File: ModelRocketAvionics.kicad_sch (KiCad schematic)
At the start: 68 parts, among them P1 USB_C_Plug, Q2 AO3400A, Q3 AO3400A, SW2 SW_SPDT, U1 ICM-42605, U2 W25Q16JVSS, U3 BMP280, U5 STM32F411, U6 L86-M33, U7 915MHz, U9 AP7361C-33E, X1 Shenzhen SCTF Elec SX2B12.000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

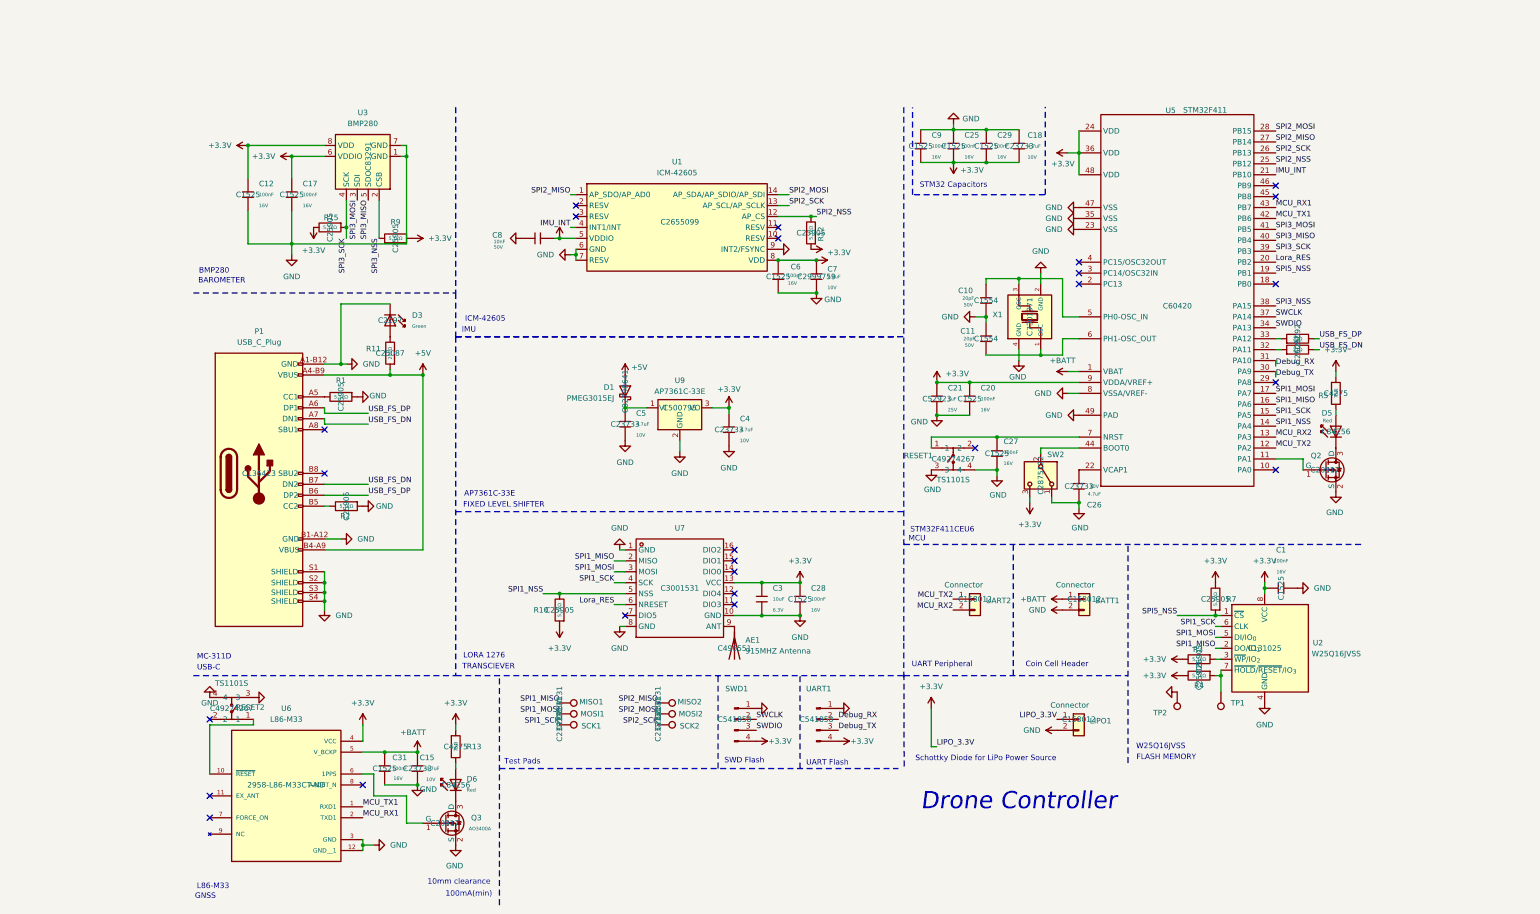
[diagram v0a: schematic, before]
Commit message: Basic layout and routing, modified schematic, and directory
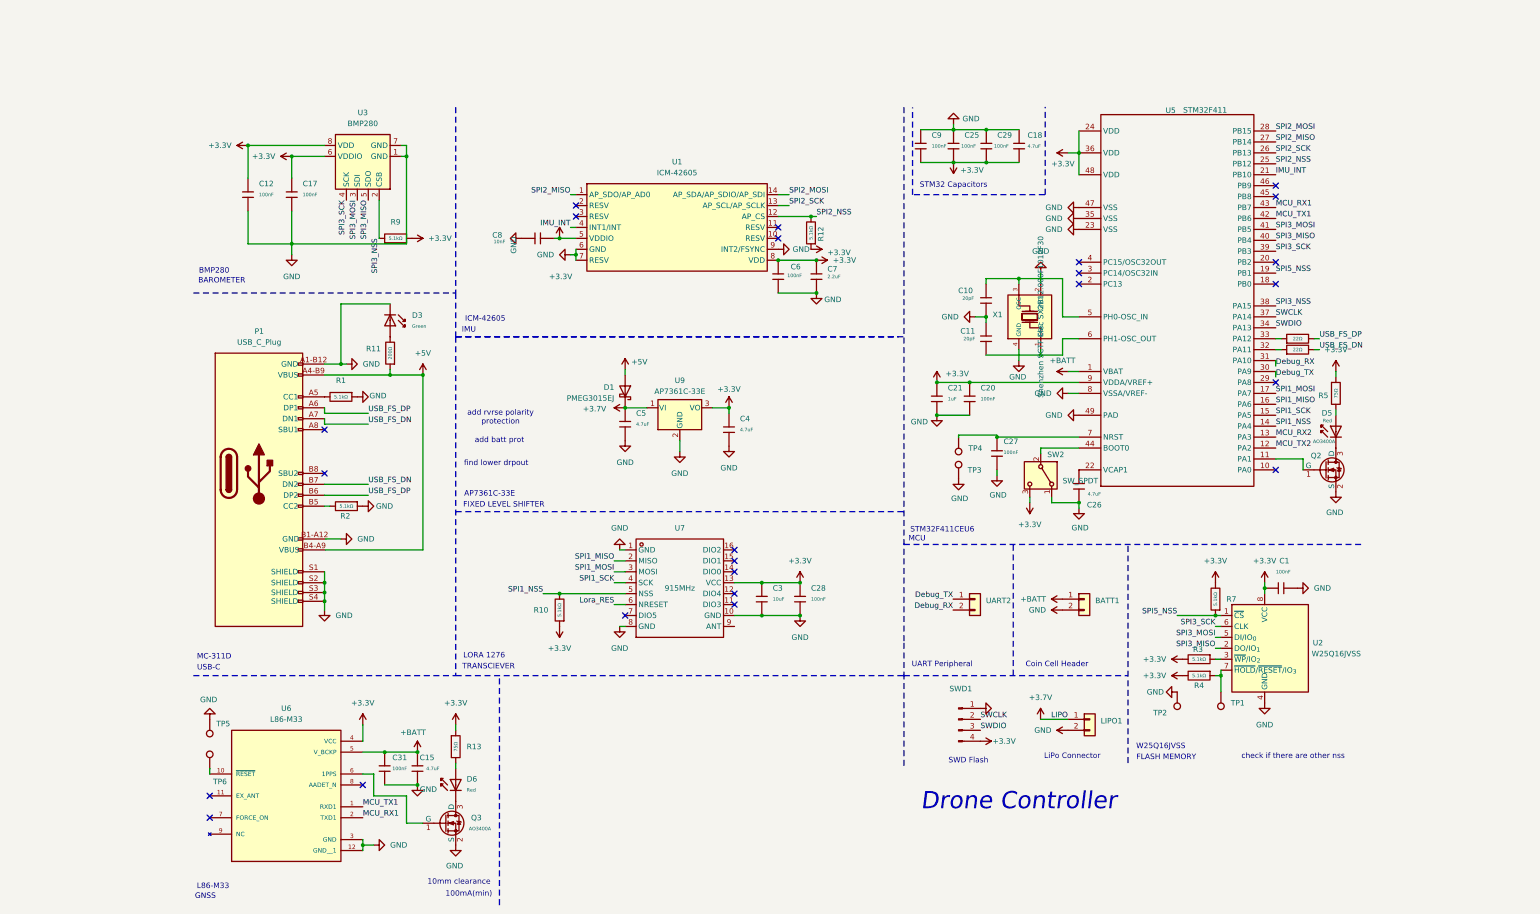
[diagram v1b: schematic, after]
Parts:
- removed AE1: 915MHZ Antenna, Connector_Coaxial:SMA_BAT_Wireless_BWSMA-KWE-Z001, symbol Device:Antenna
- removed MISO1, MISO2, MOSI1, MOSI2, SCK1, SCK2: TestPoint, TestPoint:TestPoint_Keystone_5019_Miniature, symbol Connector:TestPoint
- removed R15: 5.1kΩ, PCM_JLCPCB:R_0402, symbol PCM_JLCPCB-Resistors:0402,5.1kΩ
- removed RESET1, RESET2: TS1101S, easyeda2kicad:SW-SMD_4P-L4.5-W4.5-P3.15-LS7.5-TL, symbol easyeda2kicad:TS1101S-4.5X4.5X5.5FSS
- removed UART1: Conn_01x04_Pin, Connector_PinHeader_2.00mm:PinHeader_1x04_P2.00mm_Vertical, symbol Connector:Conn_01x04_Pin
- added TP3, TP4, TP5, TP6: TestPoint, symbol Connector:TestPoint
- P1: footprint USB-C:USB-C -> Connector_USB:USB_C_Receptacle_GCT_USB4105-xx-A_16P_TopMnt_Horizontal
- R1, R10, R11, R12, R14, R2, R3, R4, R6, R7, R9: footprint PCM_JLCPCB:R_0402 -> Resistor_SMD:R_0402_1005Metric
- R13, R5: footprint PCM_JLCPCB:R_0603 -> Resistor_SMD:R_0603_1608Metric
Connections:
- net +3.3V: no longer LIPO1.1 (Pin_1)
- net Debug_RX: now also UART2.2 (Pin_2)
- net Debug_TX: now also UART2.1 (Pin_1)
- net GND: now also TP3.1, TP5.1
- net Lora_RES: no longer U5.20 (PB2)
- net MCU_RX2: no longer UART2.2 (Pin_2)
- net MCU_TX2: no longer UART2.1 (Pin_1)
- net SPI1_MISO: no longer U2.2 (DO/IO_{1})
- net SPI1_MOSI: no longer U2.5 (DI/IO_{0})
- net SPI1_SCK: no longer U2.6 (CLK)
- net SPI3_MISO: now also U2.2 (DO/IO_{1})
- net SPI3_MOSI: now also U2.5 (DI/IO_{0})
- net SPI3_SCK: now also U2.6 (CLK)
- net at C27.1, U5.7 (NRST): now also TP4.1
- net +3.7V: now reaches C5.1, D1.1 (K), U9.1 (VI)
- net +3.7V: now also LIPO1.1 (Pin_1)
- net at U6.10 (~{RESET}): now also TP6.1
- no-connect marks 25 -> 24
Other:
- note added: "LiPo Connector"
- note added: "add batt prot"
- note added: "add rvrse polarity protection"
- note added: "check if there are other nss"
- note added: "find lower drpout"
- note removed: "Schottky Diode for LiPo Power Source"
- note removed: "Test Pads"
- note removed: "UART Flash"
- moved on the sheet: LIPO1, SWD1

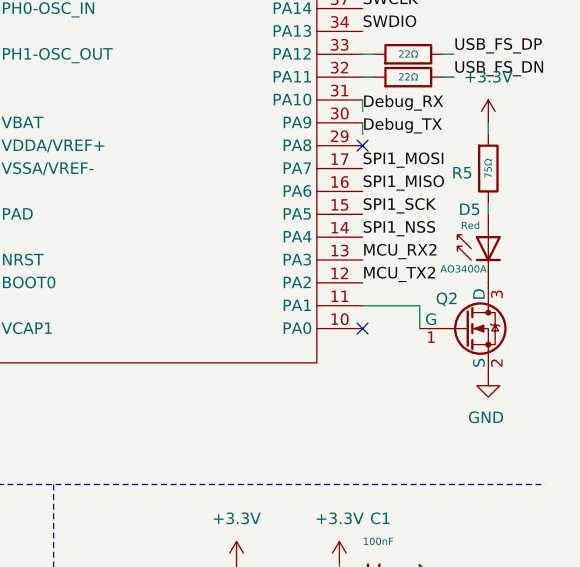
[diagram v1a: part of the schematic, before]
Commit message: Added more room for antenna pin on LoRa
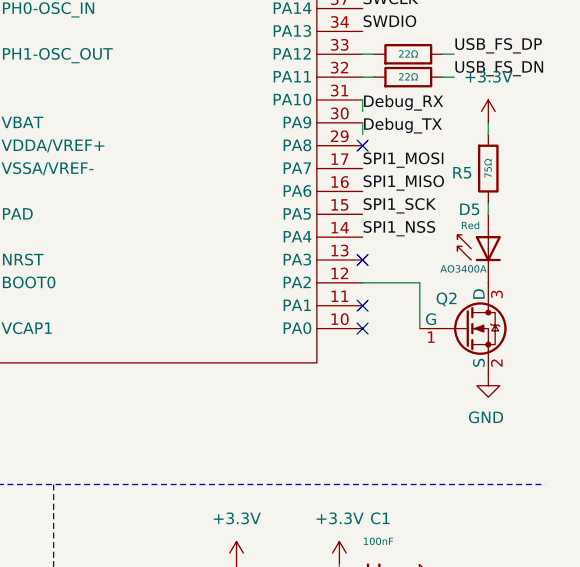
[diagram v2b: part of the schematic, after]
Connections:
- net at U5.11 (PA1): no longer Q2.1 (G)
- net MCU_RX2: no longer names the net of U5.13 (PA3)
- net MCU_TX2: no longer names the net of U5.12 (PA2)
- net MCU_TX2: now also Q2.1 (G)
- no-connect marks 24 -> 26
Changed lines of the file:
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@@
+	)
+	(no_connect
+		(at 264.1968 94.4382)
 	)
 	(no_connect
@@
 	)
 	(no_connect
+		(at 264.1968 89.3582)
+	)
+	(no_connect
 		(at 148.59 43.18)
 	)
@@
 	(wire
 		(pts
-			(xy 264.1968 94.4382) (xy 270.5468 94.4382)
-		)
-		(stroke
-			(width 0)
-			(type default)
-		)
-	)
-	(wire
-		(pts
 			(xy 111.76 115.57) (xy 113.03 115.57)
 		)
@@
 	(wire
 		(pts
-			(xy 270.5468 96.9782) (xy 270.5468 94.4382)
-		)
-		(stroke
-			(width 0)
-			(type default)
-		)
-	)
-	(wire
-		(pts
 			(xy 185.4568 84.2782) (xy 193.0768 84.2782)
 		)
@@
 		)
 	)
+	(wire
+		(pts
+			(xy 270.5468 91.8982) (xy 270.5468 96.9782)
+		)
+		(stroke
+			(width 0)
+			(type default)
+		)
+	)
 	(polyline
 		(pts
@@
 		(pts
 			(xy 204.5068 52.5282) (xy 214.6668 52.5282)
+		)
+		(stroke
+			(width 0)
+			(type default)
+		)
+	)
+	(wire
+		(pts
+			(xy 270.5468 91.8982) (xy 264.1968 91.8982)
 		)
 		(stroke
@@
 		)
 	)
-	(label "MCU_RX2"
-		(at 264.1968 89.3582 0)
-		(effects
-			(font
-				(size 1.27 1.27)
-			)
-			(justify left bottom)
-		)
-	)
 	(label "SPI1_SCK"
 		(at 110.49 123.19 180)
@@
 		(effects
 			(font
-				(size 1.27 1.27)
-			)
-			(justify left bottom)
-		)
-	)
-	(label "MCU_TX2"
-		(at 264.1968 91.8982 0)
-		(effects
-			(font

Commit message: Added RP2040 compatible branch, addded battery protection circuitry
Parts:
- removed C10, C11: 20pF, PCM_JLCPCB:C_0402, symbol PCM_JLCPCB-Capacitors:0402,20pF
- removed C18, C26: 4.7uF, PCM_JLCPCB:C_0402, symbol PCM_JLCPCB-Capacitors:0402,4.7uF
- removed C21: 1uF, PCM_JLCPCB:C_0402, symbol PCM_JLCPCB-Capacitors:0402,1uF
- removed C27: 100nF, PCM_JLCPCB:C_0402, symbol PCM_JLCPCB-Capacitors:0402,100nF
- removed D5: Red, PCM_JLCPCB:D_0805, symbol PCM_JLCPCB-Diodes:LED,0805,Red
- removed Q2: AO3400A, PCM_JLCPCB:Q_SOT-23, symbol PCM_JLCPCB-Transistors:NMOS,AO3400A
- removed R14, R6: 22Ω, Resistor_SMD:R_0402_1005Metric, symbol PCM_JLCPCB-Resistors:0402,22Ω
- removed R3, R4: 5.1kΩ, Resistor_SMD:R_0402_1005Metric, symbol PCM_JLCPCB-Resistors:0402,5.1kΩ
- removed R5: 75Ω, Resistor_SMD:R_0603_1608Metric, symbol PCM_JLCPCB-Resistors:0603,75Ω
- removed TP3, TP4: TestPoint, symbol Connector:TestPoint
- removed U5: STM32F411, Package_DFN_QFN:QFN-48-1EP_7x7mm_P0.5mm_EP5.6x5.6mm, symbol STM32:STM32F411CEU6
- removed X1: Shenzhen SCTF Elec SX2B12.000F1010F30, Crystal:Crystal_SMD_2520-4Pin_2.5x2.0mm, symbol PCM_JLCPCB-Crystals:Crystal, 12MHz, 20pF
- added C10, C11: 15pF, PCM_JLCPCB:C_0402, symbol PCM_JLCPCB-Capacitors:0402,15pF
- added C13, C14, C16, C18, C19, C2: 100nF, PCM_JLCPCB:C_0402, symbol PCM_JLCPCB-Capacitors:0402,100nF
- added C22, C23: 1uF, PCM_JLCPCB:C_0402, symbol PCM_JLCPCB-Capacitors:0402,1uF
- added D2: Red, PCM_JLCPCB:D_0805, symbol PCM_JLCPCB-Diodes:LED,0805,Red
- added JP1: Jumper_2_Open, symbol Jumper:Jumper_2_Open
- added Q1: AO3400A, PCM_JLCPCB:Q_SOT-23, symbol PCM_JLCPCB-Transistors:NMOS,AO3400A
- added Q2: NCE8205, easyeda2kicad:SOT-23-6_L2.9-W1.6-P0.95-LS2.8-BL, symbol easyeda2kicad:NCE8205
- added R16: 75Ω, Resistor_SMD:R_0603_1608Metric, symbol PCM_JLCPCB-Resistors:0603,75Ω
- added R17, R18: 27Ω, PCM_JLCPCB:R_0603, symbol PCM_JLCPCB-Resistors:0603,27Ω
- added R3: FM2113_C2832124, easyeda2kicad:SOT-23-6_L2.9-W1.6-P0.95-LS2.8-BR, symbol easyeda2kicad:FM2113_C2832124
- added R4: 2kΩ, PCM_JLCPCB:R_0402, symbol PCM_JLCPCB-Resistors:0402,2kΩ
- added U4: RP2040, Package_DFN_QFN:QFN-56-1EP_7x7mm_P0.4mm_EP3.2x3.2mm, symbol MCU_RaspberryPi:RP2040
- added X1: Crystal_GND24_Small, Crystal:Crystal_SMD_3225-4Pin_3.2x2.5mm, symbol Device:Crystal_GND24_Small
- C20: LCSC (none) -> C1525; LCSC Part Number C1525 -> (none); Manufacturer (none) -> Samsung Electro-Mechanics; Minimum Qty (none) -> 20; Stock 24076106 -> 20208285
- SWD1: footprint Connector_PinHeader_2.00mm:PinHeader_1x04_P2.00mm_Vertical -> Connector_PinHeader_2.00mm:PinHeader_2x02_P2.00mm_Vertical
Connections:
- net SPI2_SCK is gone; now on net SPI1_SCK: U1.13 (AP_SCL/AP_SCLK)
- net SPI3_NSS is gone; now on net SPI0_CSn: R9.1, U3.2 (CSB)
- net +3.3V: now also C25.1, C29.1, C9.1, C13.1, C14.1, C16.1, C2.1, C23.1, R16.1, U4.1 (IOVDD), U4.10 (IOVDD), U4.22 (IOVDD), U4.33 (IOVDD), U4.42 (IOVDD), U4.43 (ADC_AVDD), U4.44 (VREG_IN), U4.48 (USB_VDD), U4.49 (IOVDD); no longer C20.1, C25.2, C29.2, C9.2, R7.2
- net GND: now also C25.2, C29.2, C9.2, C10.1, C11.1, C13.2, C14.2, C16.2, C18.2, C19.2, C2.2, C22.2, C23.2, JP1.1 (A), Q1.2 (S), Q2.3 (S2), R4.2, U4.19 (TESTEN), U4.57 (GND), X1.2, X1.4; no longer C20.2, C25.1, C29.1, C9.1, LIPO1.2 (Pin_2)
- net SPI1_SCK: now also U4.13 (GPIO10), U4.38 (GPIO26_ADC0); no longer U7.4 (SCK)
- net SWCLK: now also U4.24 (SWCLK)
- net SWDIO: now also U4.25 (SWD)
- net USB_FS_DN: now also R18.1
- net USB_FS_DP: now also R17.1
- net QSPI_SD3: now reaches TP1.1, U2.7 (~{HOLD}/~{RESET}/IO_{3})
- net QSPI_SD3: now also U4.51 (QSPI_SD3)
- net at SW2.2 (B): now also U4.26 (RUN)
- net QSPI_SD2: now reaches U2.3 (~{WP}/IO_{2})
- net QSPI_SD2: now also U4.54 (QSPI_SD2)
- net +3.7V renamed +1S LiPo
- net +1S LiPo: now also C20.2, R3.5 (VDD)
- net MCU_RX1 renamed UART0_RX
- net UART0_RX: now also U4.16 (GPIO13)
- net MCU_TX1 renamed UART0_TX
- net UART0_TX: now also U4.15 (GPIO12)
- net SPI1_MISO renamed SPI0_RX
- net SPI0_RX: now also U3.5 (SDO), U4.2 (GPIO0), U4.27 (GPIO16), U4.31 (GPIO20), U4.6 (GPIO4)
- net SPI1_MOSI renamed SPI0_TX
- net SPI0_TX: now also U3.3 (SDI), U4.30 (GPIO19), U4.35 (GPIO23), U4.5 (GPIO3), U4.9 (GPIO7)
- net SPI1_NSS renamed SPI0_CSn
- net SPI0_CSn: now also U4.28 (GPIO17), U4.3 (GPIO1), U4.32 (GPIO21), U4.7 (GPIO5)
- net SPI2_MISO renamed SPI1_RX
- net SPI1_RX: now also U4.11 (GPIO8), U4.36 (GPIO24), U4.40 (GPIO28_ADC2)
- net SPI2_MOSI renamed SPI1_TX
- net SPI1_TX: now also U4.14 (GPIO11), U4.18 (GPIO15), U4.39 (GPIO27_ADC1)
- net SPI2_NSS renamed SPI1_CSn
- net SPI1_CSn: now also U4.12 (GPIO9), U4.37 (GPIO25), U4.41 (GPIO29_ADC3)
- net SPI3_MISO renamed QSPI_SD1
- net QSPI_SD1: now also U4.55 (QSPI_SD1); no longer U3.5 (SDO)
- net SPI3_MOSI renamed QSPI_SD0
- net QSPI_SD0: now also U4.53 (QSPI_SD0); no longer U3.3 (SDI)
- net SPI3_SCK renamed QSPI_SCLK
- net QSPI_SCLK: now also U4.52 (QSPI_SCLK); no longer U3.4 (SCK)
- net SPI5_NSS renamed QSPI_NSS
- net QSPI_NSS: now also U4.56 (QSPI_SS)
- new net: Q2.2 (D), Q2.5 (D)
- new net: Q2.4 (G2), R3.3 (OC)
- new net: Q2.6 (G1), R3.1 (OD)
- new net: R3.2 (CS), R4.1
- new net: R17.2, U4.47 (USB_DP)
- new net: Q1.1 (G), U4.17 (GPIO14)
- new net: R18.2, U4.46 (USB_DM)
- new net: D2.2, R16.2
- new net: D2.1, Q1.3 (D)
- new net: JP1.2 (B), R7.2
- new net +1V1: C18.1, C19.1, C22.1, U4.23 (DVDD), U4.45 (VREG_VOUT), U4.50 (DVDD)
- new net -1S LiPo: C20.1, LIPO1.2 (Pin_2), Q2.1 (S1), R3.6 (VSS)
- new net SPI0_SCK: U3.4 (SCK), U4.29 (GPIO18), U4.34 (GPIO22), U4.4 (GPIO2), U4.8 (GPIO6), U7.4 (SCK)
- new net XIN: C11.2, U4.20 (XIN), X1.3
- new net XOUT: C10.2, U4.21 (XOUT), X1.1
- no-connect marks 26 -> 16
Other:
- note added: "Battery Protection IC"
- note added: "RP2040"
- note added: "double check is resittor can be 5.1k for BOM"
- note removed: "STM32 Capacitors"
- note removed: "STM32F411CEU6"
- moved on the sheet: C25, C29, C6, C7, C8, C9, R12, R9, SW2, U1

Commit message: Overhauled layout, added more clearance for antenna.
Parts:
- removed UART2: Connector, easyeda2kicad:CONN-TH_B2B-XH-A-LF-SN, symbol Connector_Generic_MountingPin:Conn_01x02_MountingPin
- P1: NAME (none) -> USB
- U2: NAME (none) -> MEMORY
- U3: NAME (none) -> BAROMETER
- U4: NAME (none) -> MCU
- U6: NAME (none) -> GPS
- U7: NAME (none) -> TRANSCIEVER
- U9: NAME (none) -> LDO
- renumbered SW2 to SW1
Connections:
- net GND: now also SWD1.2 (Pin_2); no longer SWD1.1 (Pin_1)
- net IMU_INT: now also U4.35 (GPIO23), U4.41 (GPIO29_ADC3)
- net SPI0_CSn: now also R12.2, U1.12 (AP_CS); no longer R9.1, U3.2 (CSB)
- net SPI0_RX: now also U1.1 (AP_SDO/AP_AD0); no longer U3.5 (SDO)
- net SPI0_SCK: now also U1.13 (AP_SCL/AP_SCLK); no longer U3.4 (SCK)
- net SPI0_TX: now also U1.14 (AP_SDA/AP_SDIO/AP_SDI); no longer U3.3 (SDI), U4.35 (GPIO23)
- net SPI1_CSn: now also R9.1, U3.2 (CSB); no longer R12.2, U1.12 (AP_CS), U4.41 (GPIO29_ADC3)
- net SPI1_RX: now also U3.5 (SDO); no longer U1.1 (AP_SDO/AP_AD0)
- net SPI1_SCK: now also U3.4 (SCK); no longer U1.13 (AP_SCL/AP_SCLK)
- net SPI1_TX: now also U3.3 (SDI); no longer U1.14 (AP_SDA/AP_SDIO/AP_SDI)
- net SWCLK: now also SWD1.3 (Pin_3); no longer SWD1.2 (Pin_2)
- net SWDIO: now also SWD1.1 (Pin_1); no longer SWD1.3 (Pin_3)
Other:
- note added: "rserarch abt chip selct pins"
- moved on the sheet: SWD1
